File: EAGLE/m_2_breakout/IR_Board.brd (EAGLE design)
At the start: 73.6 x 93.7 mm, 38 parts, among them X1 C-GRID-14-70543, X10 C-GRID-02-70553, X11 C-GRID-02-70553, X12 C-GRID-02-70553, X2 C-GRID-14-70543, X3 C-GRID-02-70553, X4 C-GRID-02-70553, X5 C-GRID-02-70553, X6 C-GRID-02-70553, X7 C-GRID-02-70553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

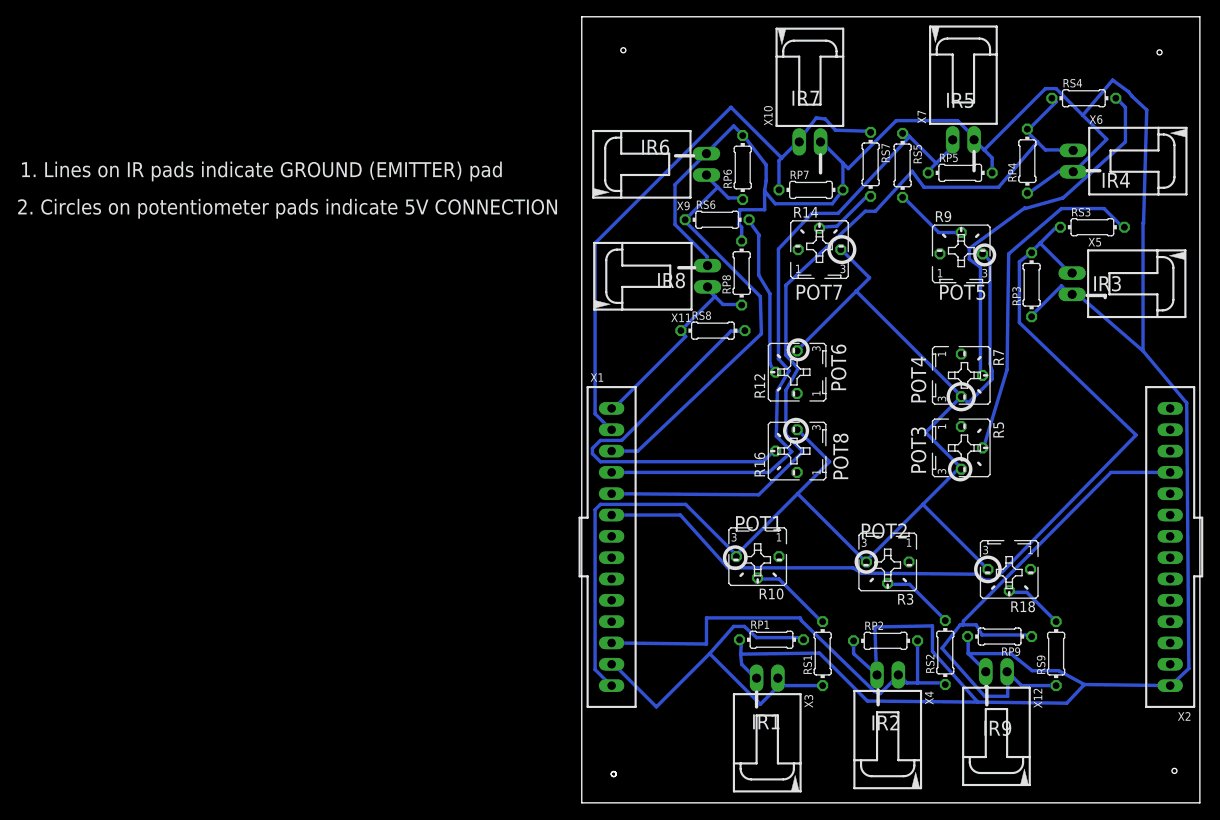
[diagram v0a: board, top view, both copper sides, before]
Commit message: Updated IR board: thicker traces, correct potentiometer, more extended pads for arduino shield headers.
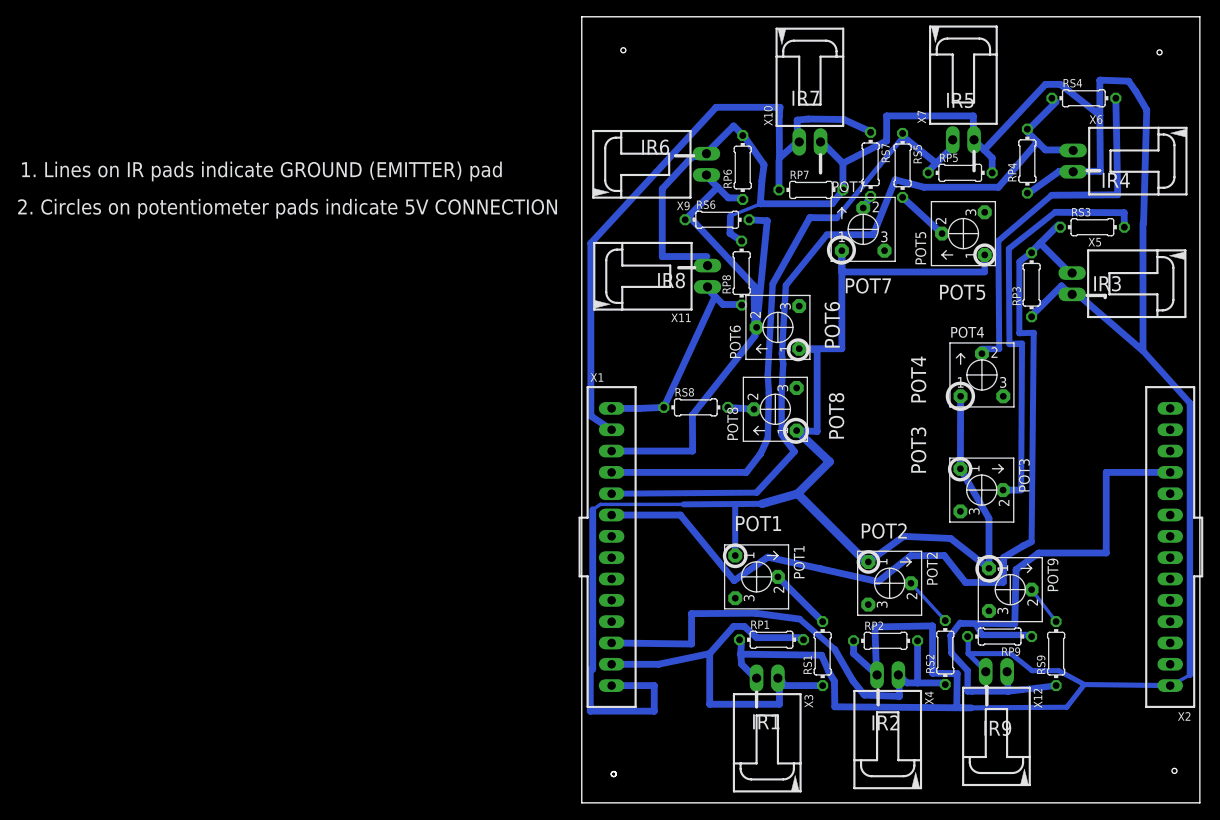
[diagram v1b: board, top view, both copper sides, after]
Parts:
- removed R10, R12, R14, R16, R18, R3, R5, R7, R9: (no value), pot:B25P
- added POT1, POT2, POT3, POT4, POT5, POT6, POT7, POT8, POT9: POTENTIOMETER_1, ben_kramer:POTENTIOMETER_1
- moved RS8 9.37 mm to (13.6, 47.1)
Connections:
- removed net POT1: R10.S, RS1.2
- removed net POT2: R3.S, RS2.2
- removed net POT3: R5.S, RS3.2
- removed net POT4: R7.S, RS4.2
- removed net POT5: R9.S, RS5.2
- removed net POT6: R12.S, RS6.2
- removed net POT7: R14.S, RS7.2
- removed net POT8: R16.S, RS8.2
- removed net POT9: R18.S, RS9.2
- new net N$1: POT1.2, RS1.2
- new net N$2: POT3.2, RS3.2
- new net N$3: POT2.2, RS2.2
- new net N$4: POT5.2, RS5.2
- new net N$5: POT6.2, RS6.2
- new net N$6: POT7.2, RS7.2
- new net N$7: POT9.2, RS9.2
- new net N$8: POT8.2, RS8.2
- new net N$9: POT4.2, RS4.2
- net 5V: now also POT1.1, POT2.1, POT3.1, POT4.1, POT5.1, POT6.1, POT7.1, POT8.1, POT9.1; no longer R10.E, R12.E, R14.E, R16.E, R18.E, R3.E, R5.E, R7.E, R9.E
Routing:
- net N$2: track 0.00 -> 49.4 mm
- net POT8: track 47.4 -> 0.00 mm
- net POT4: track 44.6 -> 0.00 mm
- net N$9: track 0.00 -> 43.3 mm
- net POT3: track 40.3 -> 0.00 mm
- net POT6: track 19.2 -> 0.00 mm
- net GND: track 323.5 -> 341.3 mm
- net 5V: track 168.7 -> 183.7 mm
- net N$5: track 0.00 -> 14.9 mm
- net POT1: track 9.98 -> 0.00 mm
- net POT2: track 8.75 -> 0.00 mm
- net POT5: track 8.70 -> 0.00 mm
- net IR9: track 65.0 -> 73.4 mm
- net POT7: track 7.58 -> 0.00 mm
- net N$1: track 0.00 -> 7.54 mm
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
